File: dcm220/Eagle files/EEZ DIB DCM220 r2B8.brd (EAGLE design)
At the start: 155 x 95 mm, 247 parts, among them IC1 Si8662AB-B-IS1, IC10 MC33272ADR2G, IC11 LT3763EFE#PBF, IC12 MC33274ADR2G, IC13 LT3763EFE#PBF, IC2 TPS54060DGQ, IC3 Si8641AB-B-IS1, IC4 M24C32-WMN6P, IC5 LP2985-33DBVR, IC6 74HC2G04GW,125, IC7 N.C., IC8 STM32F373C8T6, IC9 TL431B, J1 4907, J2 571-0500, J3 571-0100, J4 571-0500, J5 571-0100, Q1 BSP716NH6327XTSA1, Q10 BSS84, Q2 NTD5867NLT4G, Q3 NTD5867NLT4G, Q4 BSS205NH6327XTSA1, Q5 BSS84, Q6 BSP716NH6327XTSA1, Q7 NTD5867NLT4G, Q8 NTD5867NLT4G, Q9 BSS205NH6327XTSA1, X1 39-30-1020, X2 77317-104-28LF, X3 N.C., X4 DS1024-2*5R0, Y1 LF XTAL026392

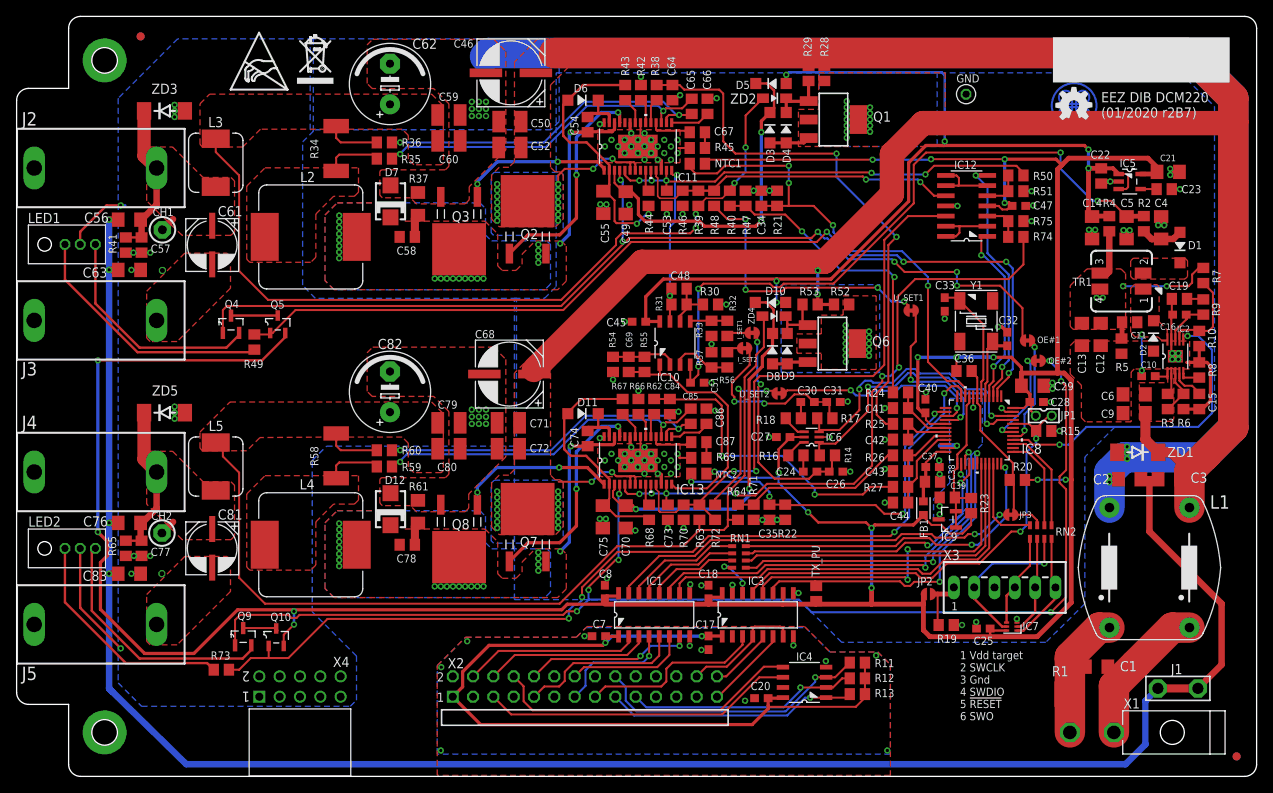
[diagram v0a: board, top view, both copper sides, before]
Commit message: DCM220 OE pull-down added
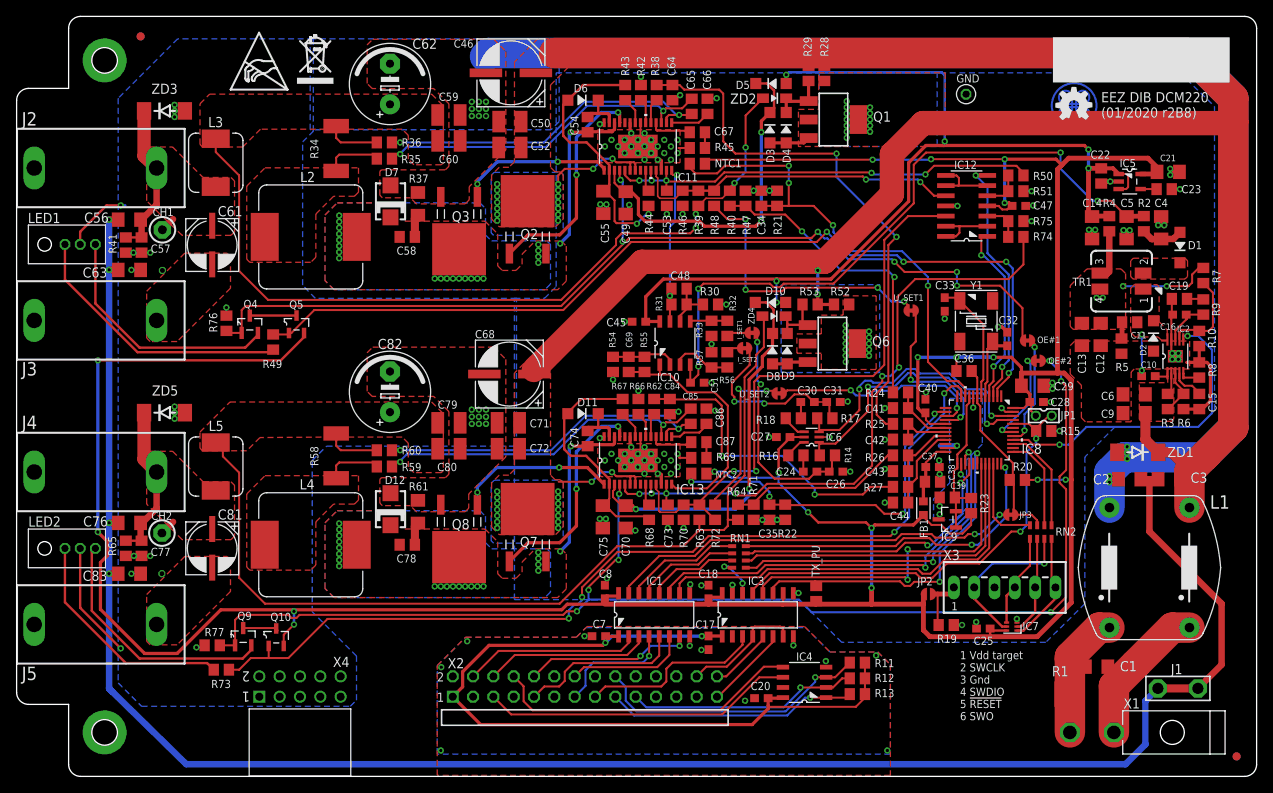
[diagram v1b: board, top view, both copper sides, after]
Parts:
- added R76, R77: 47K, rcl:R0805
- moved R49 2.35 mm to (32.1, 54.3)
- moved Q4 2.35 mm to (29.1, 56.5)
- moved Q5 2.35 mm to (35.0, 56.5)
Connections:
- net GND: now also R76.2, R77.2
- net OE#1: now also R76.1
- net OE#2: now also R77.1
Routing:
- net CC_LED#1: track 118.8 -> 116.4 mm
- net N$27: track 28.5 -> 30.9 mm
- net N$11: track 32.1 -> 34.4 mm
- net +3V3: track 440.7 -> 443.0 mm
- net GND: track 301.7 -> 304.0 mm, vias 154 -> 156
- net OE#2: track 158.0 -> 159.9 mm
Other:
- board text added: "EEZ DIB DCM220 (01/2020 r2B8)"
- board text added: "EEZ DIB DCM220 (01/2020 r2B8) Project source code: github.com/eez-open"
- board text removed: "EEZ DIB DCM220 (01/2020 r2B7)"
- board text removed: "EEZ DIB DCM220 (01/2020 r2B7) Project source code: github.com/eez-open"

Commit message: DCM220 HSE removed
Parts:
- C32, C33: value 4p7 -> N.C.
- Y1: value LF XTAL026392 -> N.C.
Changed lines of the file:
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@@
 <layer number="20" name="Dimension" color="4" fill="1" visible="yes" active="yes"/>
 <layer number="21" name="tPlace" color="7" fill="1" visible="yes" active="yes"/>
-<layer number="22" name="bPlace" color="6" fill="1" visible="yes" active="yes"/>
+<layer number="22" name="bPlace" color="6" fill="1" visible="no" active="yes"/>
 <layer number="23" name="tOrigins" color="15" fill="1" visible="yes" active="yes"/>
 <layer number="24" name="bOrigins" color="15" fill="1" visible="no" active="yes"/>
@@
 <layer number="111" name="111" color="7" fill="1" visible="no" active="no"/>
 <layer number="112" name="tSilk" color="7" fill="1" visible="no" active="no"/>
-<layer number="113" name="ReferenceLS" color="7" fill="1" visible="yes" active="yes"/>
+<layer number="113" name="ReferenceLS" color="7" fill="1" visible="no" active="yes"/>
 <layer number="114" name="EEZ" color="7" fill="1" visible="no" active="yes"/>
 <layer number="116" name="Patch_BOT" color="7" fill="1" visible="no" active="no"/>
@@
 <attribute name="VALUE" x="41.7703" y="47.5742" size="1.016" layer="27" ratio="10"/>
 </element>
-<element name="Y1" library="EEZ_Lib1" package="12SMX(B)" value="LF XTAL026392" x="119.9515" y="56.896" smashed="yes" rot="R270">
+<element name="Y1" library="EEZ_Lib1" package="12SMX(B)" value="N.C." x="119.9515" y="56.896" smashed="yes" rot="R270">
 <attribute name="NAME" x="119.2055" y="60.8965" size="1.016" layer="25" ratio="10"/>
-<attribute name="VALUE" x="120.4595" y="52.6575" size="0.8128" layer="27" ratio="10" rot="R90"/>
+<attribute name="VALUE" x="119.015" y="54.61" size="0.8128" layer="27" ratio="10"/>
 </element>
-<element name="C32" library="rcl" package="C0603" value="4p7" x="123.825" y="54.6735" smashed="yes" rot="R270">
+<element name="C32" library="rcl" package="C0603" value="N.C." x="123.825" y="54.6735" smashed="yes" rot="R270">
 <attribute name="NAME" x="122.7455" y="56.515" size="1.016" layer="25" ratio="10"/>
 <attribute name="VALUE" x="124.1425" y="53.6575" size="0.8128" layer="27" ratio="10" rot="R90"/>
 </element>
-<element name="C33" library="rcl" package="C0603" value="4p7" x="116.0145" y="58.9915" smashed="yes" rot="R90">
+<element name="C33" library="rcl" package="C0603" value="N.C." x="116.0145" y="58.9915" smashed="yes" rot="R90">
 <attribute name="NAME" x="114.808" y="60.8965" size="1.016" layer="25" ratio="10"/>
 <attribute name="VALUE" x="116.332" y="58.039" size="0.8128" layer="27" ratio="10" rot="R90"/>
@@
 <wire x1="26.2255" y1="58.6105" x2="26.2255" y2="57.592" width="0.254" layer="1"/>
 <via x="22.479" y="16.129" extent="1-16" drill="0.4" shape="square"/>
+<wire x1="22.479" y1="16.129" x2="23.4975" y2="16.129" width="0.254" layer="1"/>
+<wire x1="23.4975" y1="16.129" x2="23.4975" y2="16.383" width="0.254" layer="1"/>
 <wire x1="138.4465" y1="39.878" x2="138.811" y2="39.6875" width="0" layer="19" extent="16-16"/>
 <wire x1="116.2145" y1="41.3385" x2="116.332" y2="41.3385" width="0" layer="19" extent="16-16"/>
 <wire x1="2.2" y1="19" x2="7.945" y2="21.0745" width="0" layer="19" extent="1-1"/>
 <wire x1="2.2" y1="57" x2="7.945" y2="66.5" width="0" layer="19" extent="1-1"/>
-<wire x1="22.479" y1="16.129" x2="23.4975" y2="16.129" width="0.254" layer="1"/>
-<wire x1="23.4975" y1="16.129" x2="23.4975" y2="16.383" width="0.254" layer="1"/>
 </signal>
 <signal name="SCLK">

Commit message: FB values updated for DCP405 and DCM220
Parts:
- FB1: value 60R@100MHz -> 1K@100MHz
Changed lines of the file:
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@@
 <attribute name="VALUE" x="127.127" y="42.7355" size="1.016" layer="27" ratio="10"/>
 </element>
-<element name="FB1" library="EEZ_Lib1" package="BEAD0603" value="60R@100MHz" x="113.3475" y="33.528" smashed="yes" rot="R90">
+<element name="FB1" library="EEZ_Lib1" package="BEAD0603" value="1K@100MHz" x="113.3475" y="33.528" smashed="yes" rot="R90">
 <attribute name="NAME" x="112.884" y="32.1895" size="1.016" layer="25" ratio="10" rot="R270"/>
 <attribute name="VALUE" x="113.0875" y="34.7485" size="0.6096" layer="27" ratio="10" rot="R270"/>
